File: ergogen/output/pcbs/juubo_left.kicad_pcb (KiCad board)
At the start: 2 copper layers, 145.5 x 125.5 mm, 45 parts

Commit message: Add resistors to ergogen, add bottom case
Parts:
- added DISP1: RES_ERJ2RKF4701X, RES_ERJ2RKF4701X, F.Cu at (199.1, 86.5)
- added DISP2: RES_ERJ2RKF4701X, RES_ERJ2RKF4701X, F.Cu at (197.2, 86.5)
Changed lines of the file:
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@@
   (page A3)
   (title_block
-    (title juubo_left_no_res)
+    (title juubo_left)
     (rev v1.0.0)
     (company Unknown)
@@
         (pad 24 thru_hole circle (at 13.97 -7.62 0) (size 1.7526 1.7526) (drill 1.0922) (layers *.Cu *.SilkS *.Mask) (net 1 "P9"))
       )
+    (module RES_ERJ2RKF4701X (layer F.Cu)
+        (at 199.06 86.45 -90)
+  (descr "")
+  (attr smd)
+        (fp_text reference "DISP1" (at 1.032 -1.1564 -90) (layer F.SilkS) hide
+          (effects (font (size 0.64 0.64) (thickness 0.15)))
+        )
+  (fp_text value RES_ERJ2RKF4701X (at 5.5024 1.1564 -90) (layer F.Fab)
+    (effects (font (size 0.64 0.64) (thickness 0.15)))
+  )
+  (pad 1 smd rect (at -0.512 0.0 -90) (size 0.475 0.5) (layers F.Cu F.Mask F.Paste) (solder_mask_margin 0.102) (net 34 "VCC"))
+  (pad 2 smd rect (at 0.512 0.0 -90) (size 0.475 0.5) (layers F.Cu F.Mask F.Paste) (solder_mask_margin 0.102) (net 37 "P3"))
+  (fp_line (start -0.5 -0.25) (end -0.5 0.25) (layer F.Fab) (width 0.127))
+  (fp_line (start 0.5 -0.25) (end 0.5 0.25) (layer F.Fab) (width 0.127))
+  (fp_line (start -0.5 -0.25) (end 0.5 -0.25) (layer F.Fab) (width 0.127))
+  (fp_line (start -0.5 0.25) (end 0.5 0.25) (layer F.Fab) (width 0.127))
+  (fp_line (start -1.0 -0.5) (end -1.0 0.5) (layer F.CrtYd) (width 0.05))
+  (fp_line (start -1.0 0.5) (end 1.0 0.5) (layer F.CrtYd) (width 0.05))
+  (fp_line (start 1.0 0.5) (end 1.0 -0.5) (layer F.CrtYd) (width 0.05))
+  (fp_line (start 1.0 -0.5) (end -1.0 -0.5) (layer F.CrtYd) (width 0.05))
+)
+    (module RES_ERJ2RKF4701X (layer F.Cu)
+        (at 197.15499999999997 86.45 -90)
+  (descr "")
+  (attr smd)
+        (fp_text reference "DISP2" (at 1.032 -1.1564 -90) (layer F.SilkS) hide
+          (effects (font (size 0.64 0.64) (thickness 0.15)))
+        )
+  (fp_text value RES_ERJ2RKF4701X (at 5.5024 1.1564 -90) (layer F.Fab)
+    (effects (font (size 0.64 0.64) (thickness 0.15)))
+  )
+  (pad 1 smd rect (at -0.512 0.0 -90) (size 0.475 0.5) (layers F.Cu F.Mask F.Paste) (solder_mask_margin 0.102) (net 34 "VCC"))
+  (pad 2 smd rect (at 0.512 0.0 -90) (size 0.475 0.5) (layers F.Cu F.Mask F.Paste) (solder_mask_margin 0.102) (net 36 "P2"))
+  (fp_line (start -0.5 -0.25) (end -0.5 0.25) (layer F.Fab) (width 0.127))
+  (fp_line (start 0.5 -0.25) (end 0.5 0.25) (layer F.Fab) (width 0.127))
+  (fp_line (start -0.5 -0.25) (end 0.5 -0.25) (layer F.Fab) (width 0.127))
+  (fp_line (start -0.5 0.25) (end 0.5 0.25) (layer F.Fab) (width 0.127))
+  (fp_line (start -1.0 -0.5) (end -1.0 0.5) (layer F.CrtYd) (width 0.05))
+  (fp_line (start -1.0 0.5) (end 1.0 0.5) (layer F.CrtYd) (width 0.05))
+  (fp_line (start 1.0 0.5) (end 1.0 -0.5) (layer F.CrtYd) (width 0.05))
+  (fp_line (start 1.0 -0.5) (end -1.0 -0.5) (layer F.CrtYd) (width 0.05))
+)
     (module E73:SW_TACT_ALPS_SKQGABE010 (layer F.Cu)
         (descr "Low-profile SMD Tactile Switch, https://www.e-switch.com/product-catalog/tact/product-lines/tl3342-series-low-profile-smt-tact-switch")

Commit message: Diode pads routed
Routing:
- net P16: track 0.00 -> 21.6 mm
- net P15: track 0.00 -> 21.6 mm
- net P14: track 0.00 -> 21.6 mm
- net P10: track 0.00 -> 13.4 mm
- net layer_cluster: track 0.00 -> 4.64 mm
- net inner_home: track 0.00 -> 4.53 mm
- net space_cluster: track 0.00 -> 4.46 mm
- net ring_top: track 0.00 -> 4.32 mm
- net ring_home: track 0.00 -> 4.32 mm
- net ring_bottom: track 0.00 -> 4.32 mm
- net pinky_top: track 0.00 -> 4.32 mm
- net pinky_home: track 0.00 -> 4.32 mm
- net pinky_bottom: track 0.00 -> 4.32 mm
- net middle_top: track 0.00 -> 4.32 mm
- net middle_home: track 0.00 -> 4.32 mm
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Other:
- net class Default removed

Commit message: Matrix traces
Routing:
- net P1: track 0.00 -> 116.8 mm
- net P21: track 0.00 -> 113.7 mm
- net P20: track 0.00 -> 90.3 mm
- net P16: track 21.6 -> 107.6 mm
- net P15: track 21.6 -> 107.2 mm
- net P14: track 21.6 -> 106.9 mm
- net P10: track 13.4 -> 74.1 mm
- net P19: track 0.00 -> 38.2 mm
- net P18: track 0.00 -> 38.1 mm
- net ring_bottom: track 4.32 -> 17.7 mm
- net layer_cluster: track 4.64 -> 16.8 mm
- net extra_cluster: track 2.16 -> 14.3 mm
- net space_cluster: track 4.46 -> 16.5 mm
- net ring_home: track 4.32 -> 16.2 mm
- net middle_home: track 4.32 -> 16.1 mm
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
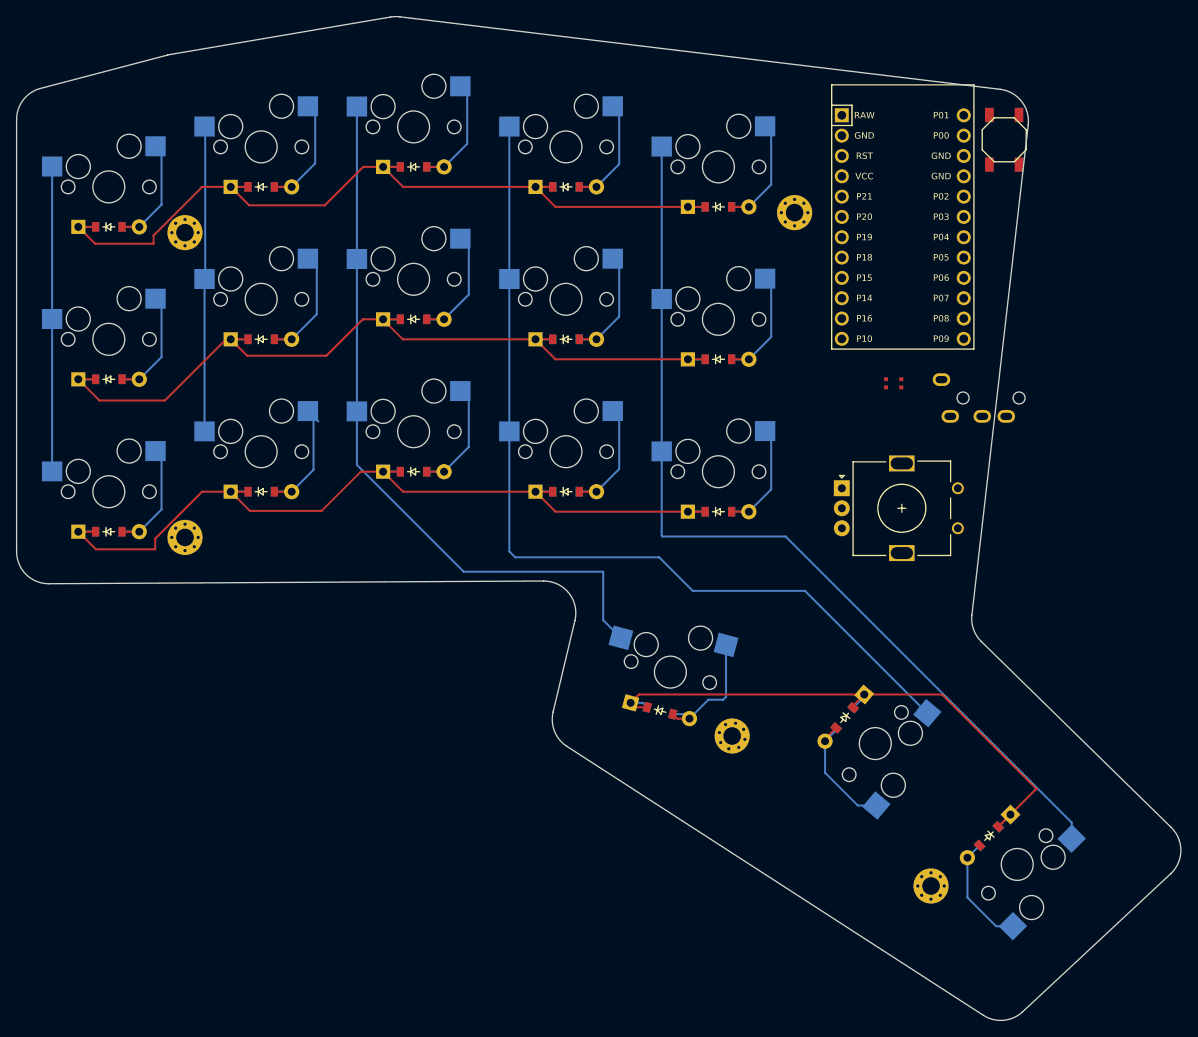
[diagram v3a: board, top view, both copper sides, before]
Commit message: Fix board, tweak mountingholes
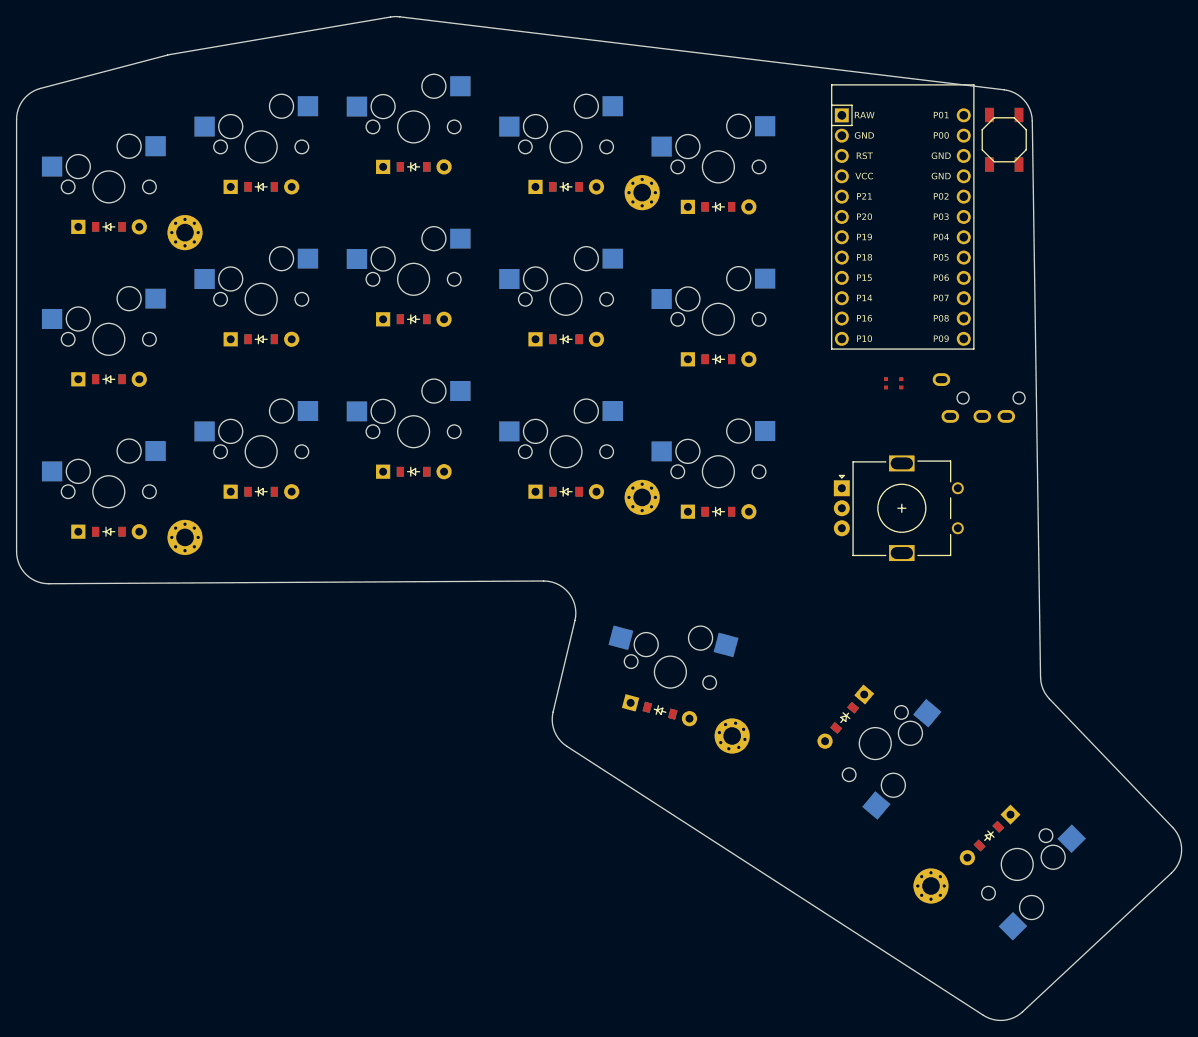
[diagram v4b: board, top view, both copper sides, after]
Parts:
- added _6: , MountingHole_2.2mm_M2_Pad_Via, F.Cu at (166.7, 100.7)
- moved _2 19.2 mm to (166.7, 62.6)
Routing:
- net P1: track 116.8 -> 0.00 mm
- net P21: track 113.7 -> 0.00 mm
- net P16: track 107.6 -> 0.00 mm
- net P15: track 107.2 -> 0.00 mm
- net P14: track 106.9 -> 0.00 mm
- net P20: track 90.3 -> 0.00 mm
- net P10: track 74.1 -> 0.00 mm
- net P19: track 38.2 -> 0.00 mm
- net P18: track 38.1 -> 0.00 mm
- net ring_bottom: track 17.7 -> 0.00 mm
- net layer_cluster: track 16.8 -> 0.00 mm
- net space_cluster: track 16.5 -> 0.00 mm
- net ring_home: track 16.2 -> 0.00 mm
- net middle_home: track 16.1 -> 0.00 mm
- net middle_bottom: track 16.1 -> 0.00 mm
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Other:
- board size 145.5 x 125.5 mm -> 145.6 x 125.5 mm
- net class Default added: clearance 0.2, trace_width 0.25, via_dia 0.8, via_drill 0.4

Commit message: Ready for routing
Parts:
- added JST1: , JST_PH_S2B-PH-K_02x2.00mm_Angled, F.Cu at (199.2, 91.1)
- added T1: , E73:SPDT_C128955, F.Cu at (199.2, 50.2)
- moved DISP2 10.7 mm to (207.6, 84.5)
- moved DISP1 10.7 mm to (209.5, 84.5)
- moved TRRS1 1.15 mm to (215.4, 91.7)
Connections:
- D1 pad 1: P16 -> P10
- D10 pad 1: P16 -> P10
- D11 pad 1: P14 -> P16
- D12 pad 1: P15 -> P14
- D13 pad 1: P16 -> P10
- D14 pad 1: P14 -> P16
- D15 pad 1: P15 -> P14
- D16 pad 1: P10 -> P6
- D17 pad 1: P10 -> P6
- D18 pad 1: P10 -> P6
- D2 pad 1: P14 -> P16
- D3 pad 1: P15 -> P14
- D4 pad 1: P16 -> P10
- D5 pad 1: P14 -> P16
- D6 pad 1: P15 -> P14
- D7 pad 1: P16 -> P10
- D8 pad 1: P14 -> P16
- D9 pad 1: P15 -> P14
- S1 pad 1: P18 -> P21
- S10 pad 1: P21 -> P18
- S11 pad 1: P21 -> P18
- S12 pad 1: P21 -> P18
- S13 pad 1: P1 -> P15
- S14 pad 1: P1 -> P15
- S15 pad 1: P1 -> P15
- S16 pad 1: P20 -> P19
- S17 pad 1: P21 -> P18
- S18 pad 1: P1 -> P15
- S2 pad 1: P18 -> P21
- S3 pad 1: P18 -> P21
- S4 pad 1: P19 -> P20
- S5 pad 1: P19 -> P20
- S6 pad 1: P19 -> P20
- S7 pad 1: P20 -> P19
- S8 pad 1: P20 -> P19
- S9 pad 1: P20 -> P19
- TRRS1 pad 2: P2 -> P3
- TRRS1 pad 3: P3 -> P2
